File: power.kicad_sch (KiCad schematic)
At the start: 11 parts, among them J1 Screw_Terminal_01x02, J3 Screw_Terminal_01x02, J4 Screw_Terminal_01x02, J5 Screw_Terminal_01x02, J6 Screw_Terminal_01x02, J7 Conn_01x05_Pin, J8 Conn_01x05_Pin, Q1 PZT2222A

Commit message: Assign footprints to resistors and use solder jumpers
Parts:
- R2, R3: footprint (none) -> Resistor_SMD:R_0805_2012Metric_Pad1.20x1.40mm_HandSolder
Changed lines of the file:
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@@
 			)
 		)
-		(property "Footprint" ""
+		(property "Footprint" "Resistor_SMD:R_0805_2012Metric_Pad1.20x1.40mm_HandSolder"
 			(at 99.06 53.848 90)
 			(effects
@@
 			)
 		)
-		(property "Footprint" ""
+		(property "Footprint" "Resistor_SMD:R_0805_2012Metric_Pad1.20x1.40mm_HandSolder"
 			(at 63.5 66.548 90)
 			(effects

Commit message: Assign footprints for the remaining components
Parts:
- J1, J3, J4, J5, J6: footprint (none) -> TerminalBlock:TerminalBlock_bornier-2_P5.08mm
- J7, J8: footprint (none) -> Connector_PinHeader_2.54mm:PinHeader_1x05_P2.54mm_Vertical
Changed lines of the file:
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@@
 			)
 		)
-		(property "Footprint" ""
+		(property "Footprint" "TerminalBlock:TerminalBlock_bornier-2_P5.08mm"
 			(at 171.45 35.56 0)
 			(effects
@@
 			)
 		)
-		(property "Footprint" ""
+		(property "Footprint" "TerminalBlock:TerminalBlock_bornier-2_P5.08mm"
 			(at 171.45 52.07 0)
 			(effects
@@
 			)
 		)
-		(property "Footprint" ""
+		(property "Footprint" "Connector_PinHeader_2.54mm:PinHeader_1x05_P2.54mm_Vertical"
 			(at 161.29 97.79 0)
 			(effects
@@
 			)
 		)
-		(property "Footprint" ""
+		(property "Footprint" "TerminalBlock:TerminalBlock_bornier-2_P5.08mm"
 			(at 171.45 68.58 0)
 			(effects
@@
 			)
 		)
-		(property "Footprint" ""
+		(property "Footprint" "TerminalBlock:TerminalBlock_bornier-2_P5.08mm"
 			(at 30.48 11.43 0)
 			(effects
@@
 			)
 		)
-		(property "Footprint" ""
+		(property "Footprint" "TerminalBlock:TerminalBlock_bornier-2_P5.08mm"
 			(at 171.45 11.43 0)
 			(effects
@@
 			)
 		)
-		(property "Footprint" ""
+		(property "Footprint" "Connector_PinHeader_2.54mm:PinHeader_1x05_P2.54mm_Vertical"
 			(at 184.15 97.79 0)
 			(effects

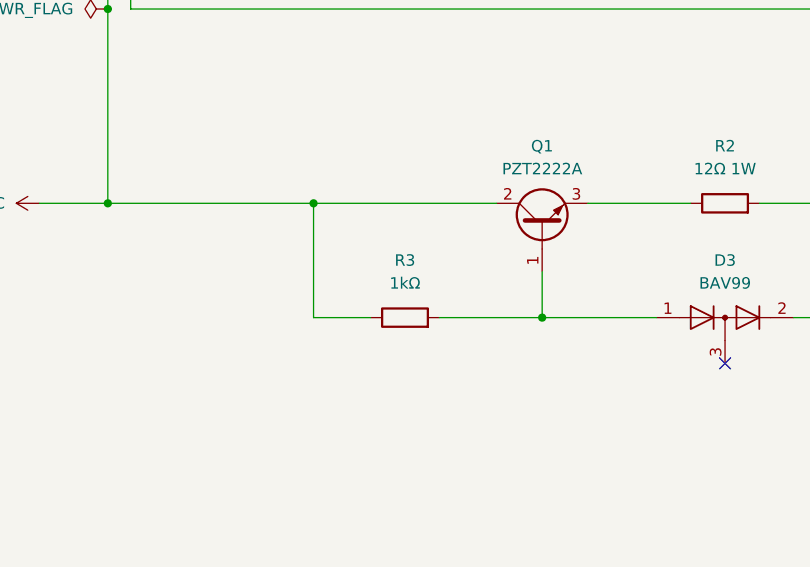
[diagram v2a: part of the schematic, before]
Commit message: Update schematic for 3.3V and specify resistor power
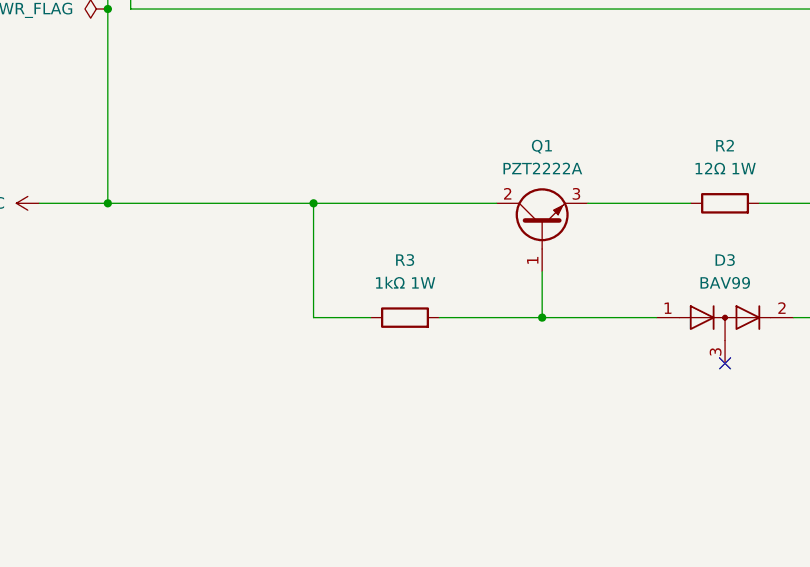
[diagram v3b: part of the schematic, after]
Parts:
- R3: value 1kΩ -> 1kΩ 1W
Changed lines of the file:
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@@
 			)
 		)
-		(property "Value" "1kΩ"
+		(property "Value" "1kΩ 1W"
 			(at 63.5 60.96 90)
 			(effects

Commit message: Place all components
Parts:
- J1: value Screw_Terminal_01x02 -> 12-22.5V DC
- J3, J4, J5, J6: value Screw_Terminal_01x02 -> 5V DC
- J7: value Conn_01x05_Pin -> 5V DC
- J8: value Conn_01x05_Pin -> GND
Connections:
- net +12-22V DC renamed +12-22.5V DC
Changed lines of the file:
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@@
-	)
-	(junction
-		(at 171.45 21.59)
-		(diameter 0)
-		(color 0 0 0 0)
-	)
-	(junction
-		(at 173.99 21.59)
-		(diameter 0)
-		(color 0 0 0 0)
 	)
 	(junction
@@
 	(wire
 		(pts
-			(xy 171.45 16.51) (xy 171.45 21.59)
-		)
-		(stroke
-			(width 0)
-			(type default)
-		)
-	)
-	(wire
-		(pts
 			(xy 173.99 100.33) (xy 173.99 102.87)
 		)
@@
 	(wire
 		(pts
-			(xy 173.99 21.59) (xy 173.99 30.48)
+			(xy 173.99 16.51) (xy 173.99 30.48)
 		)
 		(stroke
@@
 	(wire
 		(pts
-			(xy 173.99 16.51) (xy 173.99 21.59)
-		)
-		(stroke
-			(width 0)
-			(type default)
-		)
-	)
-	(wire
-		(pts
 			(xy 173.99 95.25) (xy 179.07 95.25)
 		)
@@
 	(wire
 		(pts
-			(xy 171.45 21.59) (xy 171.45 30.48)
+			(xy 171.45 16.51) (xy 171.45 30.48)
 		)
 		(stroke
@@
 			)
 		)
-		(property "Value" "Screw_Terminal_01x02"
+		(property "Value" "5V DC"
 			(at 176.53 36.8299 90)
 			(effects
@@
 			)
 		)
-		(property "Value" "Screw_Terminal_01x02"
+		(property "Value" "5V DC"
 			(at 176.53 53.3399 90)
 			(effects
@@
 			)
 		)
-		(property "Value" "Conn_01x05_Pin"
+		(property "Value" "5V DC"
 			(at 161.925 90.17 0)
 			(effects
@@
 			)
 		)
-		(property "Value" "Screw_Terminal_01x02"
+		(property "Value" "5V DC"
 			(at 176.53 69.8499 90)
 			(effects
@@
 			)
 		)
-		(property "Value" "Screw_Terminal_01x02"
+		(property "Value" "12-22.5V DC"
 			(at 35.56 12.6999 90)
 			(effects
@@
 	)
 	(symbol
-		(lib_id "power:PWR_FLAG")
-		(at 171.45 21.59 90)
-		(unit 1)
-		(exclude_from_sim no)
-		(in_bom yes)
-		(on_board yes)
-		(dnp no)
-		(fields_autoplaced yes)
-		(property "Reference" "#FLG04"
-			(at 169.545 21.59 0)
-			(effects
-				(font
-					(size 1.27 1.27)
-				)
-				(hide yes)
-			)
-		)
-		(property "Value" "PWR_FLAG"
-			(at 167.64 21.5899 90)
-			(effects
-				(font
-					(size 1.27 1.27)
-				)
-				(justify left)
-			)
-		)
-		(property "Footprint" ""
-			(at 171.45 21.59 0)
-			(effects
-				(font
-					(size 1.27 1.27)
-				)
-				(hide yes)
-			)
-		)
-		(property "Datasheet" "~"
-			(at 171.45 21.59 0)
-			(effects
-				(font
-					(size 1.27 1.27)
-				)
-				(hide yes)
-			)
-		)
-		(property "Description" "Special symbol for telling ERC where power comes from"
-			(at 171.45 21.59 0)
-			(effects
-				(font
-					(size 1.27 1.27)
-				)
-				(hide yes)
-			)
-		)
-		(pin "1"
-		)
-		(instances
-			(project "dali-pcb"
-				(path "/aa7f7e07-1f39-4222-a272-c9975d033b6d/c3d197ff-c98f-4944-adaf-f724576fcc8c"
-					(reference "#FLG04")
-					(unit 1)
-				)
-			)
-		)
-	)
-	(symbol
 		(lib_id "Device:R")
 		(at 99.06 52.07 90)
@@
 	)
 	(symbol
-		(lib_id "power:PWR_FLAG")
-		(at 173.99 21.59 270)
-		(unit 1)
-		(exclude_from_sim no)
-		(in_bom yes)
-		(on_board yes)
-		(dnp no)
-		(fields_autoplaced yes)
-		(property "Reference" "#FLG05"
-			(at 175.895 21.59 0)
-			(effects
-				(font
-					(size 1.27 1.27)
-				)
-				(hide yes)
-			)
-		)
-		(property "Value" "PWR_FLAG"
-			(at 177.8 21.5899 90)
-			(effects
-				(font
-					(size 1.27 1.27)
-				)
-				(justify left)
-			)
-		)
-		(property "Footprint" ""
-			(at 173.99 21.59 0)
-			(effects
-				(font
-					(size 1.27 1.27)
-				)
-				(hide yes)
-			)
-		)
-		(property "Datasheet" "~"
-			(at 173.99 21.59 0)
-			(effects
-				(font
-					(size 1.27 1.27)
-				)
-				(hide yes)
-			)
-		)
-		(property "Description" "Special symbol for telling ERC where power comes from"
-			(at 173.99 21.59 0)
-			(effects
-				(font
-					(size 1.27 1.27)
-				)
-				(hide yes)
-			)
-		)
-		(pin "1"
-		)
-		(instances
-			(project "dali-pcb"
-				(path "/aa7f7e07-1f39-4222-a272-c9975d033b6d/c3d197ff-c98f-4944-adaf-f724576fcc8c"
-					(reference "#FLG05")
-					(unit 1)
-				)
-			)
-		)
-	)
-	(symbol
 		(lib_id "power:+5V")
 		(at 166.37 63.5 90)
@@
 			)
 		)
-		(property "Value" "Screw_Terminal_01x02"
+		(property "Value" "5V DC"
 			(at 176.53 12.6999 90)
 			(effects
@@
 			)
 		)
-		(property "Value" "+12-22V DC"
+		(property "Value" "+12-22.5V DC"
 			(at 19.05 52.0699 90)
 			(effects
@@
 		(on_board yes)
 		(dnp no)
-		(fields_autoplaced yes)
 		(property "Reference" "J8"
-			(at 183.515 87.63 0)
-			(effects
-				(font
-					(size 1.27 1.27)
-				)
-			)
-		)
-		(property "Value" "Conn_01x05_Pin"
-			(at 183.515 90.17 0)
-			(effects
-				(font
-					(size 1.27 1.27)
-				)
-			)
-		)
+			(at 180.594 87.63 0)
+			(effects
+				(font
+					(size 1.27 1.27)
+				)
+				(justify right)
+			)
+		)
+		(property "Value" "GND"
+			(at 180.086 90.17 0)
+			(effects
+				(font
+					(size 1.27 1.27)
+				)
+				(justify right)
+			)
+		)

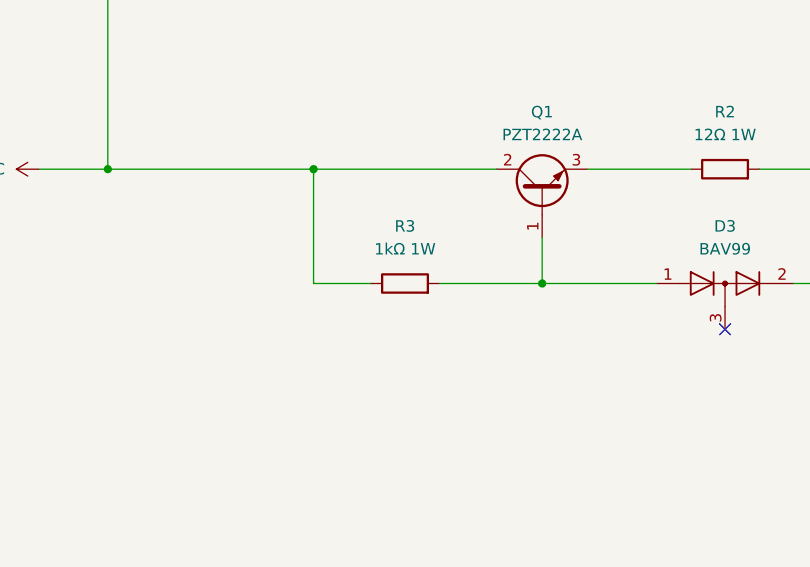
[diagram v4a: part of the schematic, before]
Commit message: Rotate R3 and improve silkscreen positions
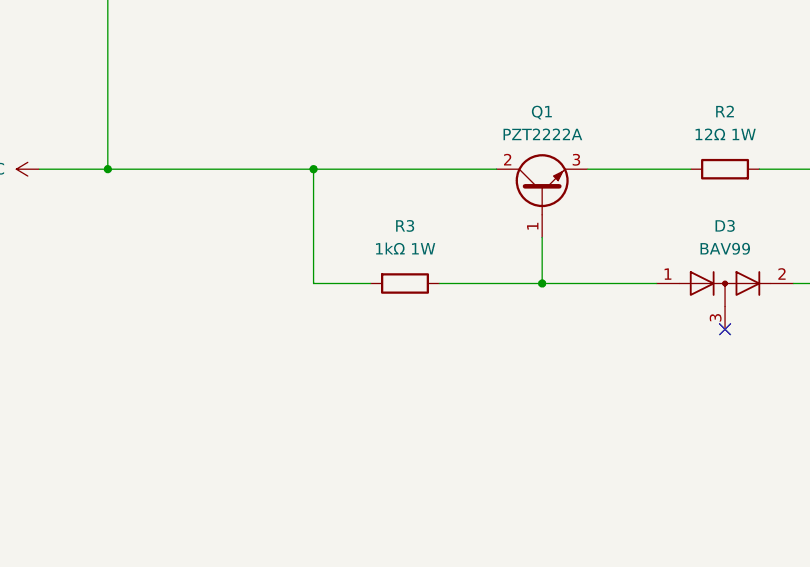
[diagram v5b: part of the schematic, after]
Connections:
- net +12-22.5V DC: now also R3.2; no longer R3.1
- net at D3.1 (K), Q1.1 (B): now also R3.1; no longer R3.2
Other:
- moved on the sheet: R3
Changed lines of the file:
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@@
 	(symbol
 		(lib_id "Device:R")
-		(at 63.5 64.77 90)
+		(at 63.5 64.77 270)
 		(unit 1)
 		(exclude_from_sim no)

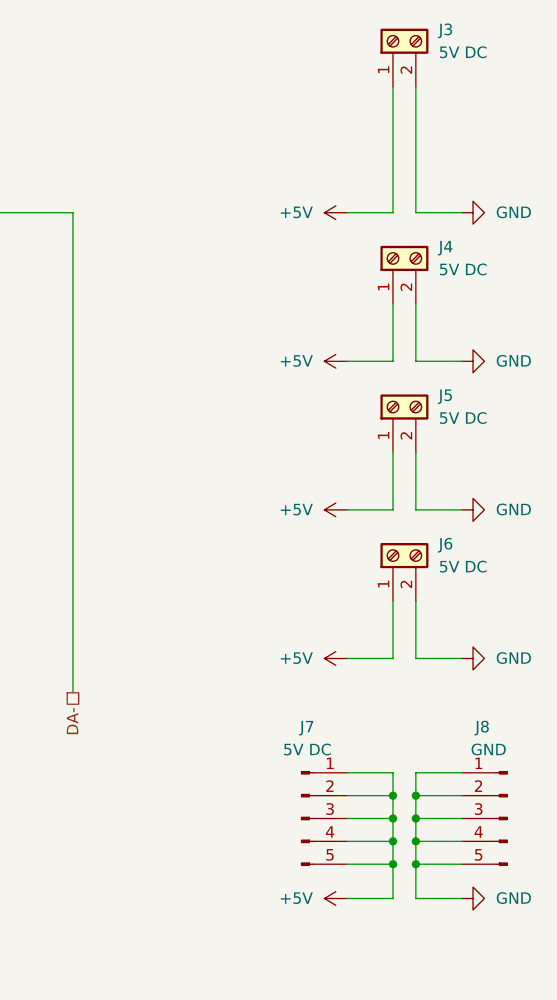
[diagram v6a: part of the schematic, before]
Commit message: Renumber references and place LOLIN-S3-MINI
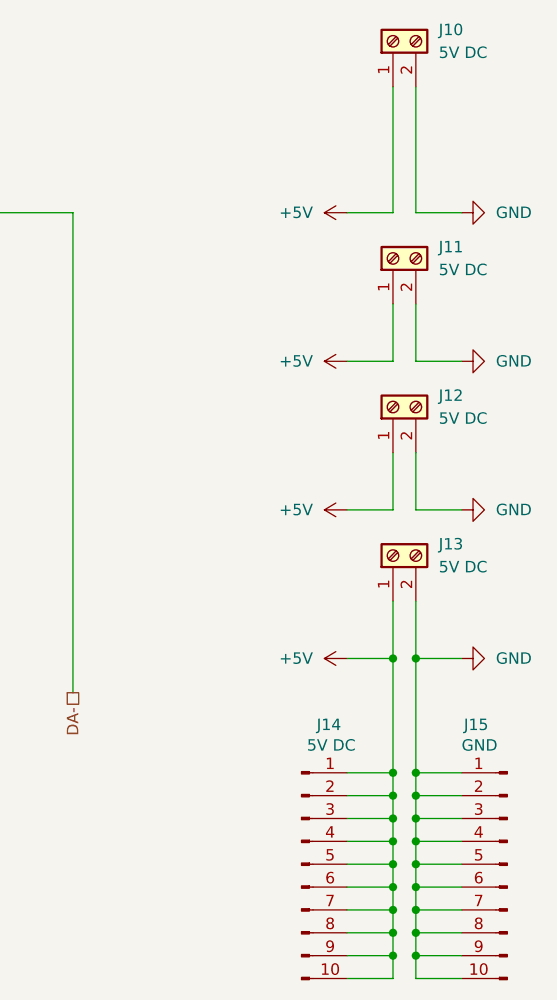
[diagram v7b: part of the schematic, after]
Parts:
- J14: renamed from J7; footprint Connector_PinHeader_2.54mm:PinHeader_1x05_P2.54mm_Vertical -> Connector_PinHeader_2.54mm:PinHeader_1x10_P2.54mm_Vertical; symbol Connector:Conn_01x05_Pin -> Connector:Conn_01x10_Pin
- J15: renamed from J8; footprint Connector_PinHeader_2.54mm:PinHeader_1x05_P2.54mm_Vertical -> Connector_PinHeader_2.54mm:PinHeader_1x10_P2.54mm_Vertical; symbol Connector:Conn_01x05_Pin -> Connector:Conn_01x10_Pin
- renumbered J3 to J10, J4 to J11, J5 to J12, J6 to J13
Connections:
- net +5V: now also J14.10 (Pin_10), J14.6 (Pin_6), J14.7 (Pin_7), J14.8 (Pin_8), J14.9 (Pin_9)
- net GND: now also J15.10 (Pin_10), J15.6 (Pin_6), J15.7 (Pin_7), J15.8 (Pin_8), J15.9 (Pin_9)

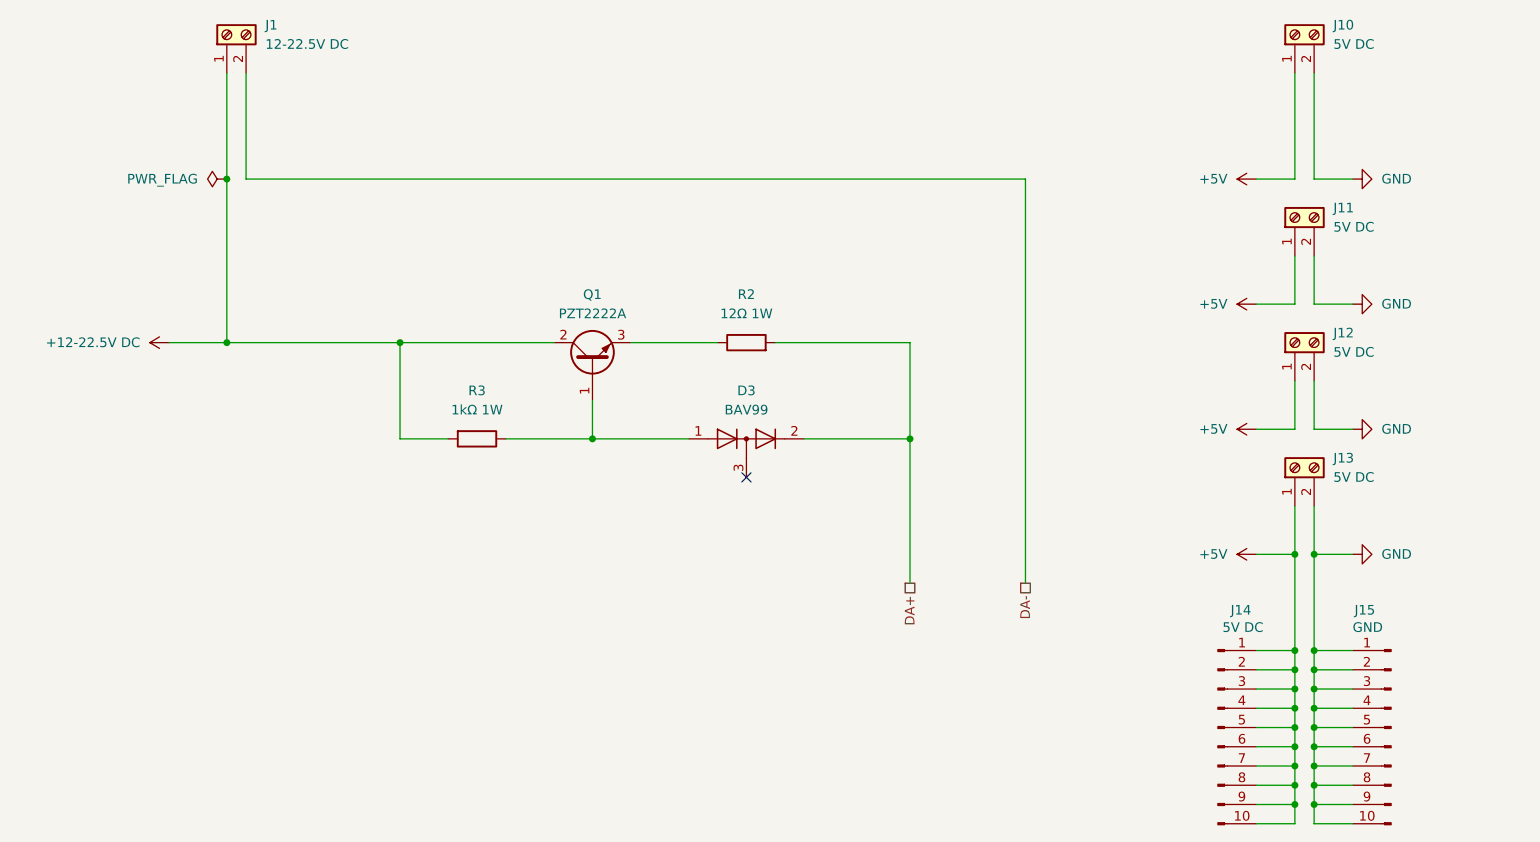
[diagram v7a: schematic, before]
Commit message: Fix screw terminal orientation and mounting holes
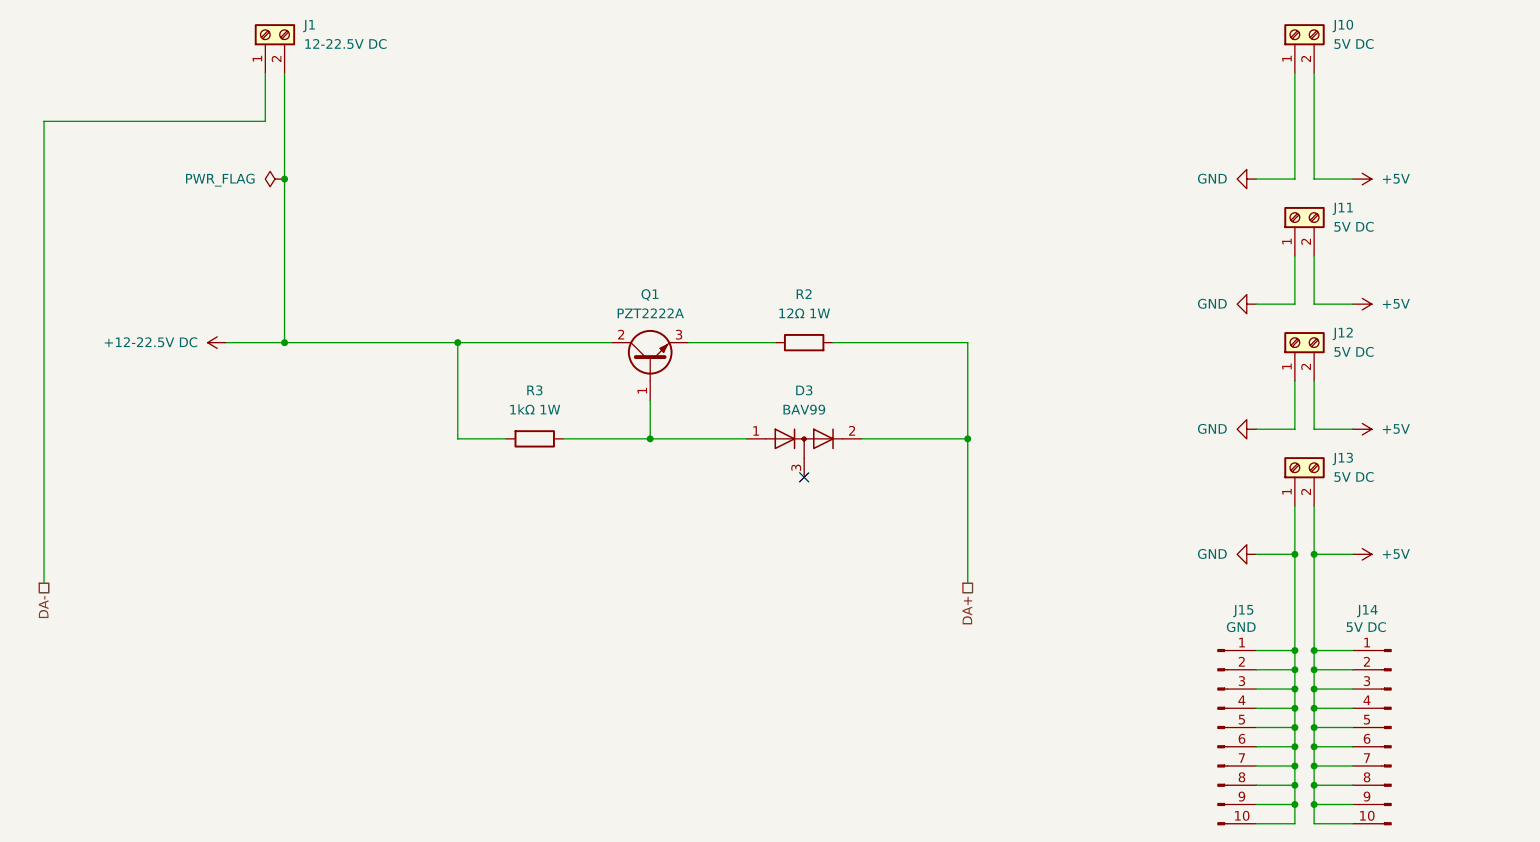
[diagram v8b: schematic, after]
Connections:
- net +12-22.5V DC: now also J1.2 (Pin_2); no longer J1.1 (Pin_1)
- net +5V: now also J10.2 (Pin_2), J11.2 (Pin_2), J12.2 (Pin_2), J13.2 (Pin_2); no longer J10.1 (Pin_1), J11.1 (Pin_1), J12.1 (Pin_1), J13.1 (Pin_1)
- net DA-: now also J1.1 (Pin_1); no longer J1.2 (Pin_2)
- net GND: now also J10.1 (Pin_1), J11.1 (Pin_1), J12.1 (Pin_1), J13.1 (Pin_1); no longer J10.2 (Pin_2), J11.2 (Pin_2), J12.2 (Pin_2), J13.2 (Pin_2)
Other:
- moved on the sheet: D3, J1, J14, J15, Q1, R2, R3
